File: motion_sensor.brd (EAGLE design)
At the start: 30 x 30 mm, 47 parts, among them J1 AVR_SPI_PRG_6PTH, J2 FTDI_DEVICERA_SMT, U1 LP2985A-33DBVTE4, U2 nRF8001, U3 ATMEGA328P_TQFP, Y1 16MHz, Y2 FC-255 32.7680K-A3, Y4 16MHz

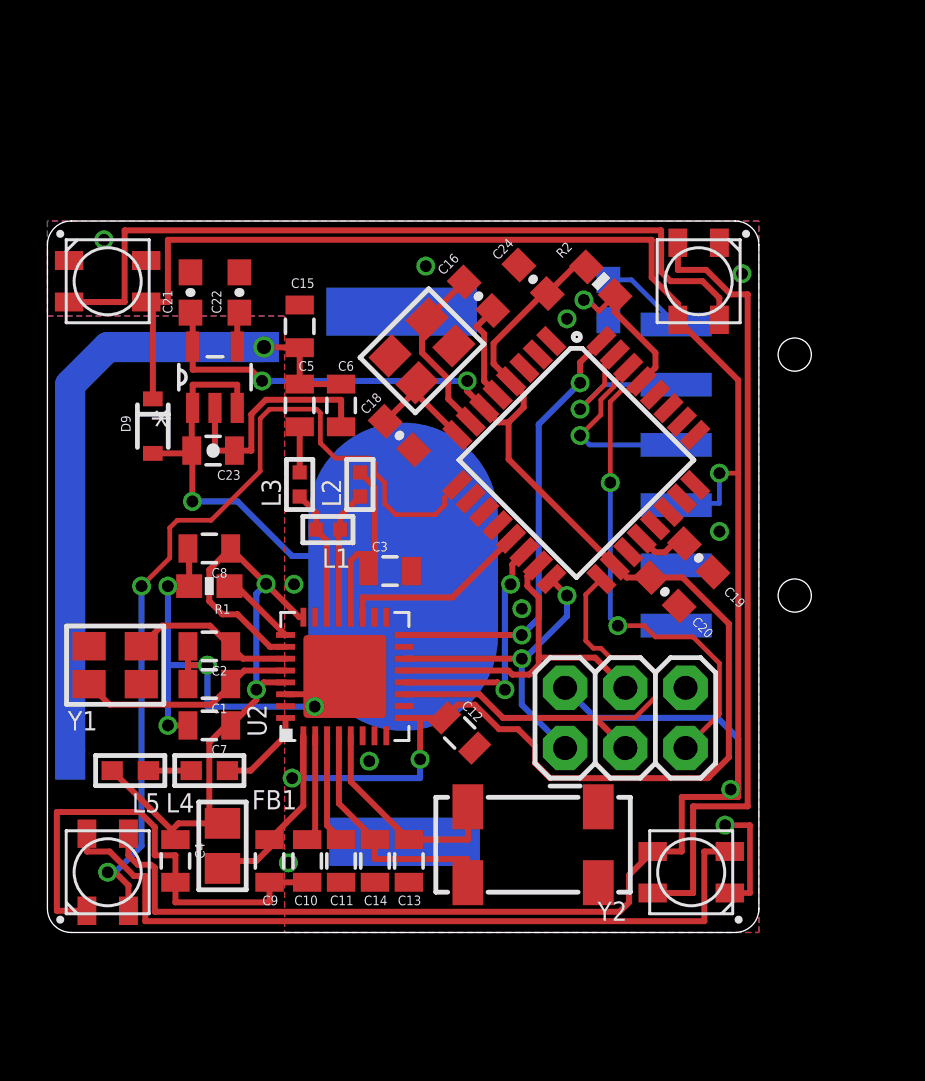
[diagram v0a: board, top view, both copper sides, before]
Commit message: Respin board to be 35mm square. Better antenna. Less things near the antenna.
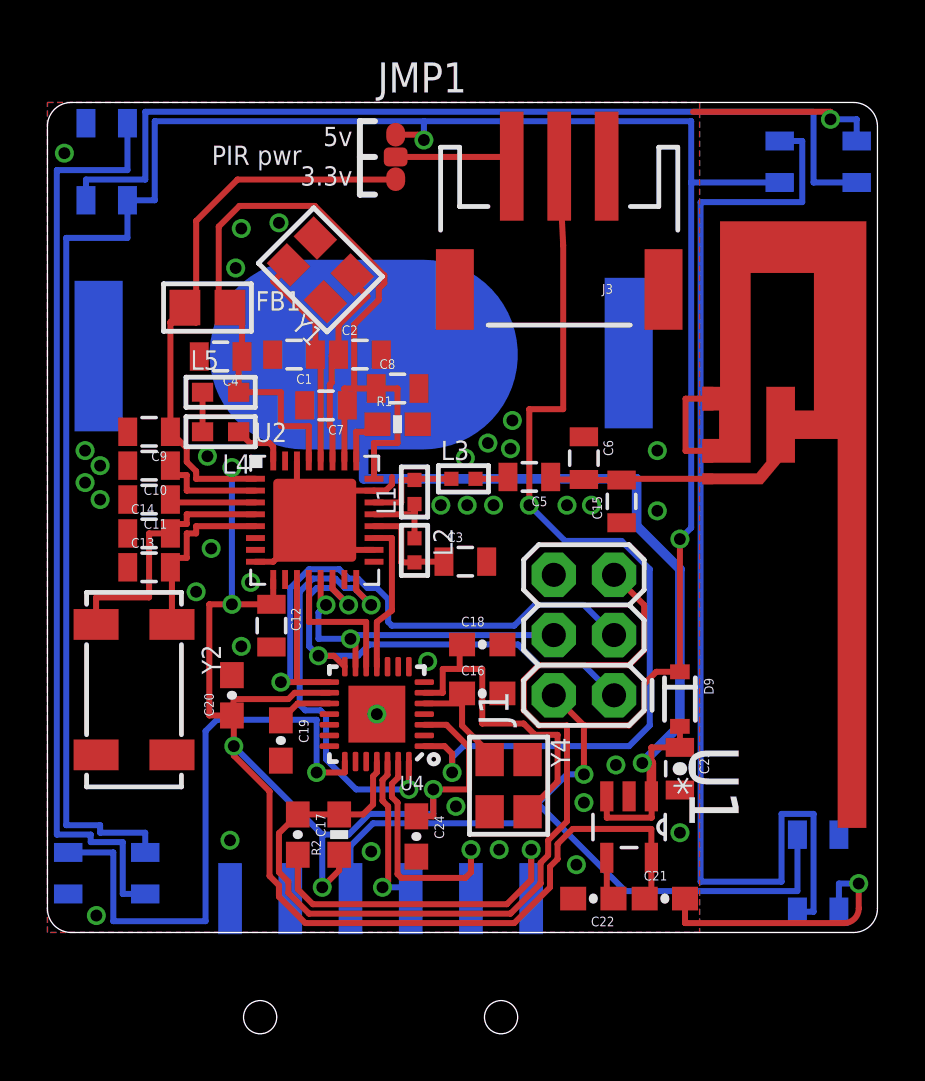
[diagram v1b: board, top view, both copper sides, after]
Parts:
- removed U$28: (no value), microbuilder:ANT_PCB_2.4GHZ_NRF8001_1.6MM_1OZ
- removed U3: ATMEGA328P_TQFP, SparkFun-DigitalIC:TQFP32-08
- added E1: ANTENNATRACE, SparkFun-RF:TRACE_ANTENNA_2.4GHZ_25.7MM
- added J3: 3-PIN SMD, SparkFun-Connectors:JST-3-SMD
- added JMP1: 0R-JUMPC, jump-0r-smd:C0R-JMP
- added U4: ATMEGA328P_VQFNVQFN, SparkFun-DigitalIC:VQFN-28
- moved U$17 39.0 mm to (32.5, 2.50), flipped to the bottom, turned to 90 degrees
- moved U$11 38.8 mm to (2.50, 32.5), flipped to the bottom, turned to 270 degrees
- moved C21 32.5 mm to (26.0, 1.43), turned to 0 degrees
- moved C22 29.6 mm to (23.0, 1.43), turned to 180 degrees
- moved J2 28.8 mm to (14.0, -3.57), turned to 0 degrees
- moved C17 26.1 mm to (10.6, 4.13), flipped to the top, turned to 270 degrees
- moved R2 25.8 mm to (12.3, 4.13), turned to 90 degrees
- moved U1 25.8 mm to (24.5, 4.45), turned to 270 degrees
- moved D9 25.0 mm to (26.7, 9.84)
- moved C24 24.0 mm to (15.6, 4.05), turned to 270 degrees
- moved C23 23.8 mm to (26.7, 6.91), turned to 270 degrees
- moved FB1 22.7 mm to (6.75, 26.4), turned to 0 degrees
- moved C4 21.4 mm to (7.30, 24.3), turned to 180 degrees
- moved C19 19.2 mm to (9.84, 8.10), turned to 270 degrees
- moved C9 18.8 mm to (4.29, 21.1), turned to 180 degrees
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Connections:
- net N$1 renamed DEC2
- net N$10 renamed XC2
- net N$11 renamed DCC
- net N$22 renamed XL2
- net N$23 renamed XL1
- net N$27 renamed BYPASS
- net N$3 renamed ???
- net N$8 renamed DEC1
- net N$9 renamed XC1
- removed net N$12: U$17.4
- removed net N$24: C19.1, U3.20
- new net AREF: C19.1, U4.17
- new net PIR: J3.2, U4.1
- new net PIR_VDD: J3.3, JMP1.2
- net 3.3V: now also JMP1.3, U4.16, U4.3; no longer U3.18, U3.4, U3.6
- net 5V: now also JMP1.1
- net BLE_RDY: now also U4.28; no longer U3.32
- net BLE_RST: now also U4.11; no longer U3.13
- net GND: now also E1.GND, E1.GND2, J3.1, U4.18, U4.4, U4.PAD; no longer U3.10, U3.21, U3.3, U3.5
- net LED: now also U4.22; no longer U3.9
- net MISO: now also U4.14; no longer U3.16
- net MOSI: now also U4.13; no longer U3.15
- net N$20: now also E1.ANT; no longer U$28.FEED
- net OSC1: now also U4.5; no longer U3.7
- net OSC2: now also U4.6; no longer U3.8
- net REQN: now also U4.12; no longer U3.14
- net RESET: now also U4.25; no longer U3.29
- net RX: now also U4.26; no longer U3.30
- net SCK: now also U4.15; no longer U3.17
- net TX: now also U4.27; no longer U3.31
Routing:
- net PIR: track 0.00 -> 40.1 mm, vias 0 -> 2
- net 5V: track 100.9 -> 127.4 mm, vias 2 -> 3
- net GND: track 62.8 -> 37.7 mm, vias 14 -> 37
- net 3.3V: track 79.6 -> 98.7 mm, vias 4 -> 5
- net V_BATT: track 20.4 -> 38.4 mm
- net N$7: track 33.6 -> 48.9 mm
- net RESET: track 28.1 -> 40.3 mm, vias 3 -> 0
- net LED: track 37.5 -> 25.5 mm, vias 2 -> 1
- net DTR: track 3.64 -> 15.3 mm, vias 0 -> 1
- net OSC2: track 4.72 -> 14.0 mm
- net AVDD: track 29.9 -> 37.6 mm, vias 2 -> 0
- net MISO: track 14.0 -> 21.0 mm
- net SCK: track 20.6 -> 27.2 mm, vias 0 -> 1
- net N$5: track 33.1 -> 39.2 mm
- net N$6: track 33.8 -> 39.2 mm
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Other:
- board size 30 x 30 mm -> 35 x 35 mm
- board text added: "3.3v"
- board text added: "5v"
- board text added: "PIR pwr"
